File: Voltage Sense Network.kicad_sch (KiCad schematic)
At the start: 4 parts

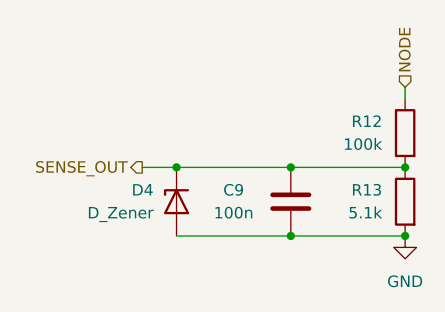
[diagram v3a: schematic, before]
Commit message: finished layout, routing, and silkscreen
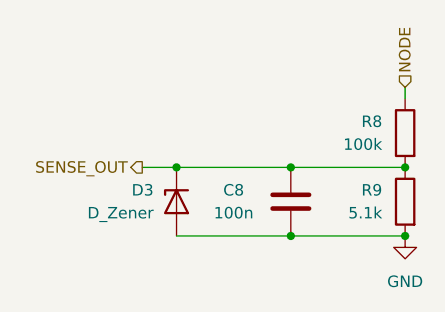
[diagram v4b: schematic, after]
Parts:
- renumbered C9 to C8, D4 to D3, R12 to R8, R13 to R9
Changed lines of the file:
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@@
 		(dnp no)
 		(fields_autoplaced yes)
-		(property "Reference" "R12"
+		(property "Reference" "R8"
 			(at 152.4 85.0899 0)
 			(show_name no)
@@
 			(project "RSC-LV3-LVBPS"
 				(path "/4bbf2fff-9f66-421d-84bf-68d1dcd1e11d/1856a03c-7c06-4d7b-bc4d-561ad22da0a9"
-					(reference "R16")
+					(reference "R14")
 					(unit 1)
 				)
 				(path "/4bbf2fff-9f66-421d-84bf-68d1dcd1e11d/89d250a3-47d9-4100-a7e9-bffe0c4542cf"
-					(reference "R14")
+					(reference "R12")
 					(unit 1)
 				)
 				(path "/4bbf2fff-9f66-421d-84bf-68d1dcd1e11d/a618e32b-dfbf-4cfb-b0df-a706c9a76794"
-					(reference "R12")
+					(reference "R8")
 					(unit 1)
 				)
@@
 		(in_pos_files yes)
 		(dnp no)
-		(property "Reference" "C9"
+		(property "Reference" "C8"
 			(at 135.89 92.71 0)
 			(show_name no)
@@
 			(project "RSC-LV3-LVBPS"
 				(path "/4bbf2fff-9f66-421d-84bf-68d1dcd1e11d/1856a03c-7c06-4d7b-bc4d-561ad22da0a9"
-					(reference "C11")
+					(reference "C10")
 					(unit 1)
 				)
 				(path "/4bbf2fff-9f66-421d-84bf-68d1dcd1e11d/89d250a3-47d9-4100-a7e9-bffe0c4542cf"
-					(reference "C10")
+					(reference "C9")
 					(unit 1)
 				)
 				(path "/4bbf2fff-9f66-421d-84bf-68d1dcd1e11d/a618e32b-dfbf-4cfb-b0df-a706c9a76794"
-					(reference "C9")
+					(reference "C8")
 					(unit 1)
 				)
@@
 		(dnp no)
 		(fields_autoplaced yes)
-		(property "Reference" "D4"
+		(property "Reference" "D3"
 			(at 127 92.7099 90)
 			(show_name no)
@@
 			(project "RSC-LV3-LVBPS"
 				(path "/4bbf2fff-9f66-421d-84bf-68d1dcd1e11d/1856a03c-7c06-4d7b-bc4d-561ad22da0a9"
+					(reference "D7")
+					(unit 1)
+				)
+				(path "/4bbf2fff-9f66-421d-84bf-68d1dcd1e11d/89d250a3-47d9-4100-a7e9-bffe0c4542cf"
 					(reference "D6")
 					(unit 1)
 				)
-				(path "/4bbf2fff-9f66-421d-84bf-68d1dcd1e11d/89d250a3-47d9-4100-a7e9-bffe0c4542cf"
-					(reference "D5")
-					(unit 1)
-				)
 				(path "/4bbf2fff-9f66-421d-84bf-68d1dcd1e11d/a618e32b-dfbf-4cfb-b0df-a706c9a76794"
-					(reference "D4")
+					(reference "D3")
 					(unit 1)
 				)
@@
 		(dnp no)
 		(fields_autoplaced yes)
-		(property "Reference" "#PWR023"
+		(property "Reference" "#PWR019"
 			(at 154.94 104.14 0)
 			(hide yes)
@@
 			(project "RSC-LV3-LVBPS"
 				(path "/4bbf2fff-9f66-421d-84bf-68d1dcd1e11d/1856a03c-7c06-4d7b-bc4d-561ad22da0a9"
-					(reference "#PWR025")
+					(reference "#PWR023")
 					(unit 1)
 				)
 				(path "/4bbf2fff-9f66-421d-84bf-68d1dcd1e11d/89d250a3-47d9-4100-a7e9-bffe0c4542cf"
-					(reference "#PWR024")
+					(reference "#PWR022")
 					(unit 1)
 				)
 				(path "/4bbf2fff-9f66-421d-84bf-68d1dcd1e11d/a618e32b-dfbf-4cfb-b0df-a706c9a76794"
-					(reference "#PWR023")
+					(reference "#PWR019")
 					(unit 1)
 				)
@@
 		(dnp no)
 		(fields_autoplaced yes)
-		(property "Reference" "R13"
+		(property "Reference" "R9"
 			(at 152.4 92.7099 0)
 			(show_name no)
@@
 			(project "RSC-LV3-LVBPS"
 				(path "/4bbf2fff-9f66-421d-84bf-68d1dcd1e11d/1856a03c-7c06-4d7b-bc4d-561ad22da0a9"
-					(reference "R17")
+					(reference "R15")
 					(unit 1)
 				)
 				(path "/4bbf2fff-9f66-421d-84bf-68d1dcd1e11d/89d250a3-47d9-4100-a7e9-bffe0c4542cf"
-					(reference "R15")
+					(reference "R13")
 					(unit 1)
 				)
 				(path "/4bbf2fff-9f66-421d-84bf-68d1dcd1e11d/a618e32b-dfbf-4cfb-b0df-a706c9a76794"
-					(reference "R13")
-					(unit 1)
-				)
+					(reference "R9")
+					(unit 1)
+				)

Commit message: r0 final
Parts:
- removed D3: D_Zener, Diode_SMD:D_SOD-323_HandSoldering, symbol Device:D_Zener
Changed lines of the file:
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@@
-	)
-	(junction
-		(at 142.24 97.79)
-		(diameter 0)
-		(color 0 0 0 0)
 	)
 	(junction
@@
 		(color 0 0 0 0)
 	)
-	(junction
-		(at 129.54 90.17)
-		(diameter 0)
-		(color 0 0 0 0)
-	)
 	(wire
 		(pts
@@
 	(wire
 		(pts
-			(xy 129.54 90.17) (xy 125.73 90.17)
-		)
-		(stroke
-			(width 0)
-			(type default)
-		)
-	)
-	(wire
-		(pts
-			(xy 142.24 97.79) (xy 129.54 97.79)
-		)
-		(stroke
-			(width 0)
-			(type default)
-		)
-	)
-	(wire
-		(pts
-			(xy 142.24 90.17) (xy 129.54 90.17)
+			(xy 125.73 90.17) (xy 142.24 90.17)
 		)
 		(stroke
@@
 					(unit 1)
 				)
-			)
-		)
-	)
-	(symbol
-		(lib_id "Device:D_Zener")
-		(at 129.54 93.98 90)
-		(mirror x)
-		(unit 1)
-		(body_style 1)
-		(exclude_from_sim no)
-		(in_bom yes)
-		(on_board yes)
-		(in_pos_files yes)
-		(dnp no)
-		(fields_autoplaced yes)
-		(property "Reference" "D3"
-			(at 127 92.7099 90)
-			(show_name no)
-			(do_not_autoplace no)
-			(effects
-				(font
-					(size 1.27 1.27)
-				)
-				(justify left)
-			)
-		)
-		(property "Value" "D_Zener"
-			(at 127 95.2499 90)
-			(show_name no)
-			(do_not_autoplace no)
-			(effects
-				(font
-					(size 1.27 1.27)
-				)
-				(justify left)
-			)
-		)
-		(property "Footprint" "Diode_SMD:D_SOD-323_HandSoldering"
-			(at 129.54 93.98 0)
-			(hide yes)
-			(show_name no)
-			(do_not_autoplace no)
-			(effects
-				(font
-					(size 1.27 1.27)
-				)
-			)
-		)
-		(property "Datasheet" ""
-			(at 129.54 93.98 0)
-			(hide yes)
-			(show_name no)
-			(do_not_autoplace no)
-			(effects
-				(font
-					(size 1.27 1.27)
-				)
-			)
-		)
-		(property "Description" "Zener diode"
-			(at 129.54 93.98 0)
-			(hide yes)
-			(show_name no)
-			(do_not_autoplace no)
-			(effects
-				(font
-					(size 1.27 1.27)
-				)
-			)
-		)
-		(pin "1"
-		)
-		(pin "2"
-		)
-		(instances
-			(project "RSC-LV3-LVBPS"
-				(path "/4bbf2fff-9f66-421d-84bf-68d1dcd1e11d/1856a03c-7c06-4d7b-bc4d-561ad22da0a9"
-					(reference "D7")
-					(unit 1)
-				)
-				(path "/4bbf2fff-9f66-421d-84bf-68d1dcd1e11d/89d250a3-47d9-4100-a7e9-bffe0c4542cf"
-					(reference "D6")
-					(unit 1)
-				)
-				(path "/4bbf2fff-9f66-421d-84bf-68d1dcd1e11d/a618e32b-dfbf-4cfb-b0df-a706c9a76794"
-					(reference "D3")
-					(unit 1)
-				)
